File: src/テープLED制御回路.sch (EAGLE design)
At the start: 26 parts

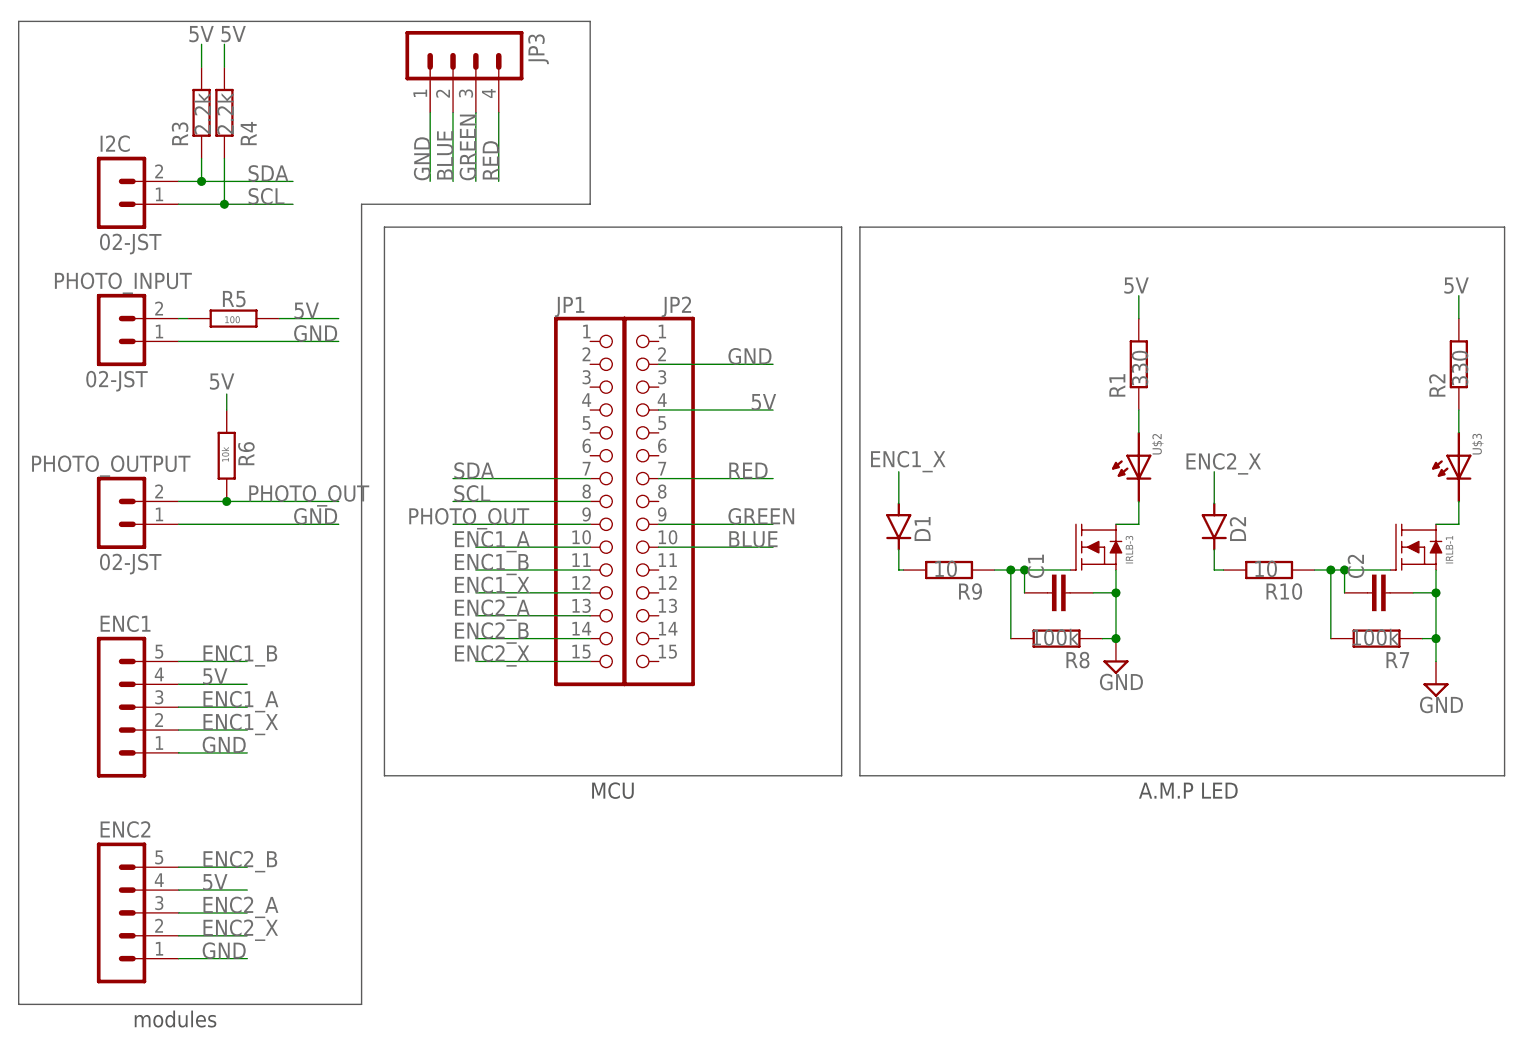
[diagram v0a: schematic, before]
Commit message: 国技館コントローラの追加
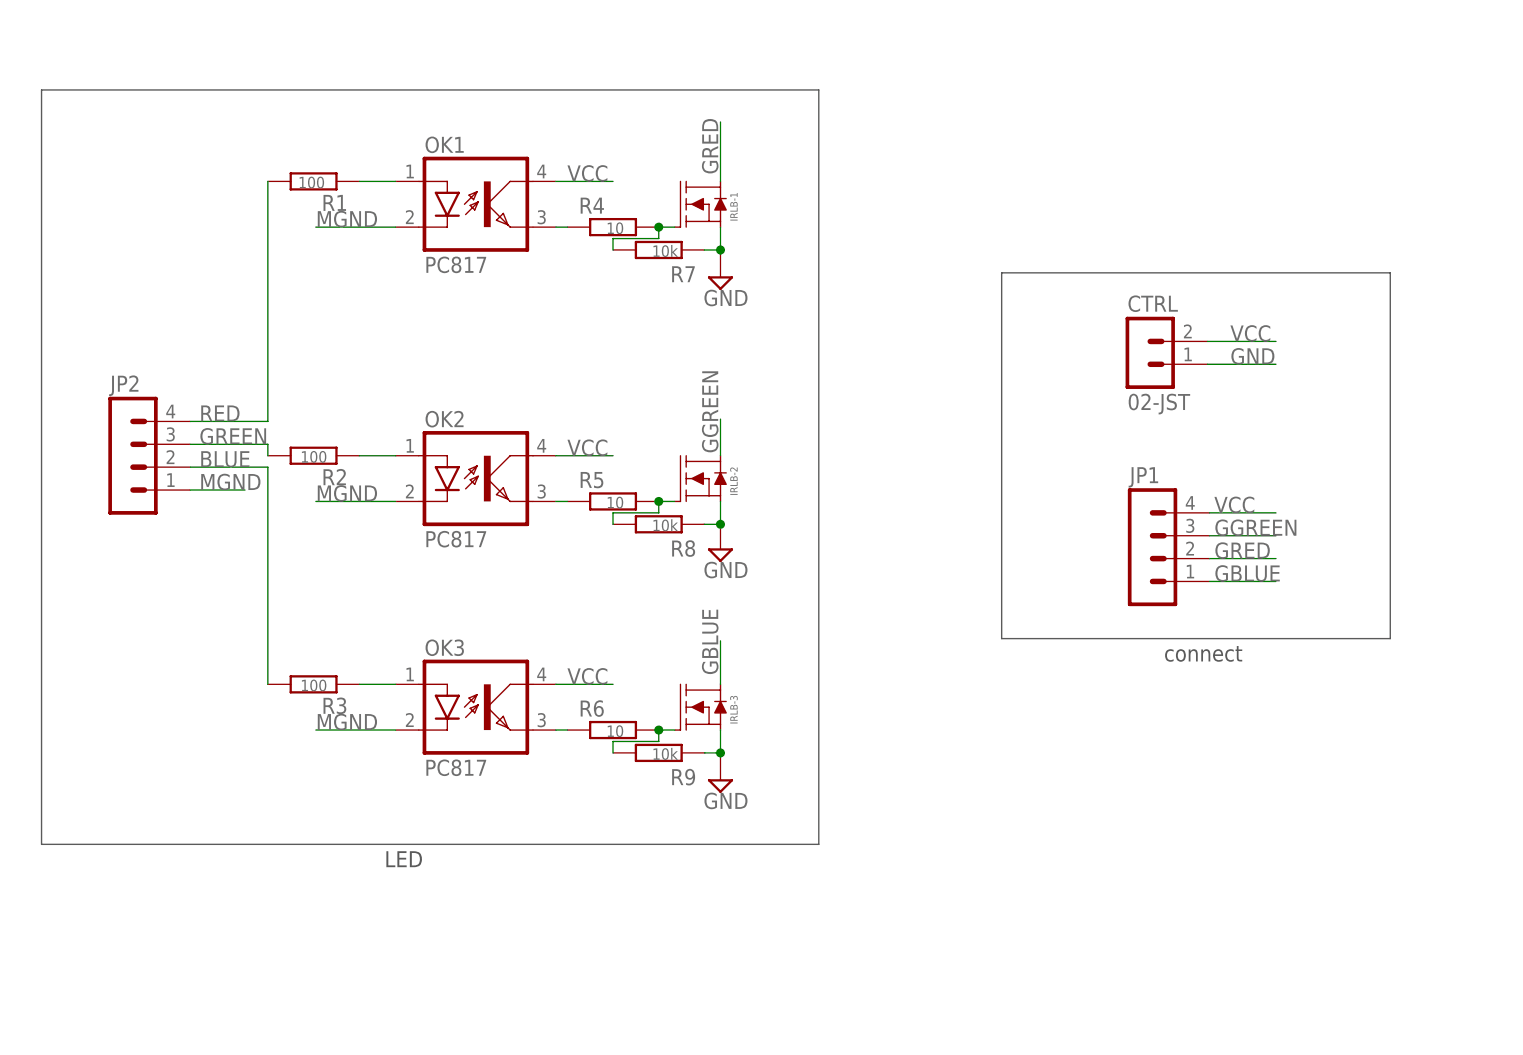
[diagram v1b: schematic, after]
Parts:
- removed C1, C2: (no value), capacitor-wima:C5/2.5
- removed D1, D2: DIODE_STAND, DIODE_STAND:DIODE_STAND
- removed ENC1, ENC2: (no value), con-jst-xh:05-JST
- removed I2C, PHOTO_INPUT, PHOTO_OUTPUT: 02-JST, con-jst-xh:02-JST
- removed JP3: (no value), con-jst-xh:04-JST
- removed R10: 10, rcl:R-EU_0207/2V
- removed U$2, U$3: LED, OKUDA_libraries:LED
- added CTRL: 02-JST, con-jst-xh:02-JST
- added IRLB-2: IRLB3813STAND, OKUDA_libraries:IRLB3813STAND
- added OK1, OK2, OK3: PC817, optocoupler:PC817
- JP1, JP2: device pinhead:PINHD-1X15 -> con-jst-xh:04-JST
- R1, R2: value 330 -> 100; device rcl:R-EU_0207/2V -> rcl:R-EU_0204/7
- R3: value 2.2k -> 100; device rcl:R-EU_0207/2V -> rcl:R-EU_0204/7
- R4: value 2.2k -> 10; device rcl:R-EU_0207/2V -> rcl:R-EU_0204/7
- R5: value 100 -> 10
- R6: value 10k -> 10
- R7, R8: value 100k -> 10k; device rcl:R-EU_0207/2V -> rcl:R-EU_0204/7
- R9: value 10 -> 10k; device rcl:R-EU_0207/2V -> rcl:R-EU_0204/7
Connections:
- removed net 5V: ENC1.4, ENC2.4, JP2.4, R1.2, R2.2, R3.2, R4.2, R5.1, R6.2
- removed net ENC1_A: ENC1.3, JP1.10
- removed net ENC1_B: ENC1.5, JP1.11
- removed net ENC1_X: D1.A, ENC1.2, JP1.12
- removed net ENC2_A: ENC2.3, JP1.13
- removed net ENC2_B: ENC2.5, JP1.14
- removed net ENC2_X: D2.A, ENC2.2, JP1.15
- removed net N$1: IRLB-3.D, U$2.C
- removed net N$2: R1.1, U$2.A
- removed net PHOTO_OUT: JP1.9, PHOTO_OUTPUT.2, R6.1
- removed net SCL: I2C.1, JP1.8, R4.1
- removed net SDA: I2C.2, JP1.7, R3.1
- new net GBLUE: IRLB-3.D, JP1.1
- new net GGREEN: IRLB-2.D, JP1.3
- new net GRED: IRLB-1.D, JP1.2
- new net MGND: JP2.1, OK1.C, OK2.C, OK3.C
- new net N$10: OK3.EMIT, R6.1
- new net N$11: IRLB-3.G, R6.2, R9.1
- new net VCC: CTRL.2, JP1.4, OK1.COL, OK2.COL, OK3.COL
- net BLUE: now also JP2.2, R3.2; no longer JP2.10, JP3.2
- net GND: now also CTRL.1, IRLB-2.S, R7.2, R8.2, R9.2; no longer C1.2, C2.2, ENC1.1, ENC2.1, JP2.2, JP3.1, PHOTO_INPUT.1, PHOTO_OUTPUT.1, R7.1, R8.1
- net GREEN: now also JP2.3, R2.2; no longer JP2.9, JP3.3
- net N$3: now also OK1.EMIT, R4.1; no longer C1.1, IRLB-3.G, R8.2, R9.1
- net N$4: now also OK1.A, R1.1; no longer C2.1, IRLB-1.G, R10.1, R7.2
- net N$5: now also OK2.A, R2.1; no longer IRLB-1.D, U$3.C
- net N$6: now also OK3.A, R3.1; no longer R2.1, U$3.A
- net N$7: now also IRLB-1.G, R4.2, R7.1; no longer PHOTO_INPUT.2, R5.2
- net N$8: now also OK2.EMIT, R5.1; no longer D1.C, R9.2
- net N$9: now also IRLB-2.G, R5.2, R8.1; no longer D2.C, R10.2
- net RED: now also JP2.4, R1.2; no longer JP2.7, JP3.4
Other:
- note added: "LED"
- note added: "connect"
- note removed: "A.M.P LED"
- note removed: "MCU"
- note removed: "modules"
- moved on the sheet: IRLB-1, IRLB-3, R1, R2, R3, R4, R5, R6, R7, R8, R9
